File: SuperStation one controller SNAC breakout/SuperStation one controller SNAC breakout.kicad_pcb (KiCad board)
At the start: 2 copper layers, 50 x 100 mm, 28 parts, among them J1 Conn_01x09_Socket, J2 Conn_01x09_Socket, J3 USB3_A, Q1 BSS138, Q2 BSS138, Q3 BSS138, Q4 BSS138, Q5 BSS138, Q6 BSS138, Q7 BSS138, U1 NCP1117-5.0_SOT223

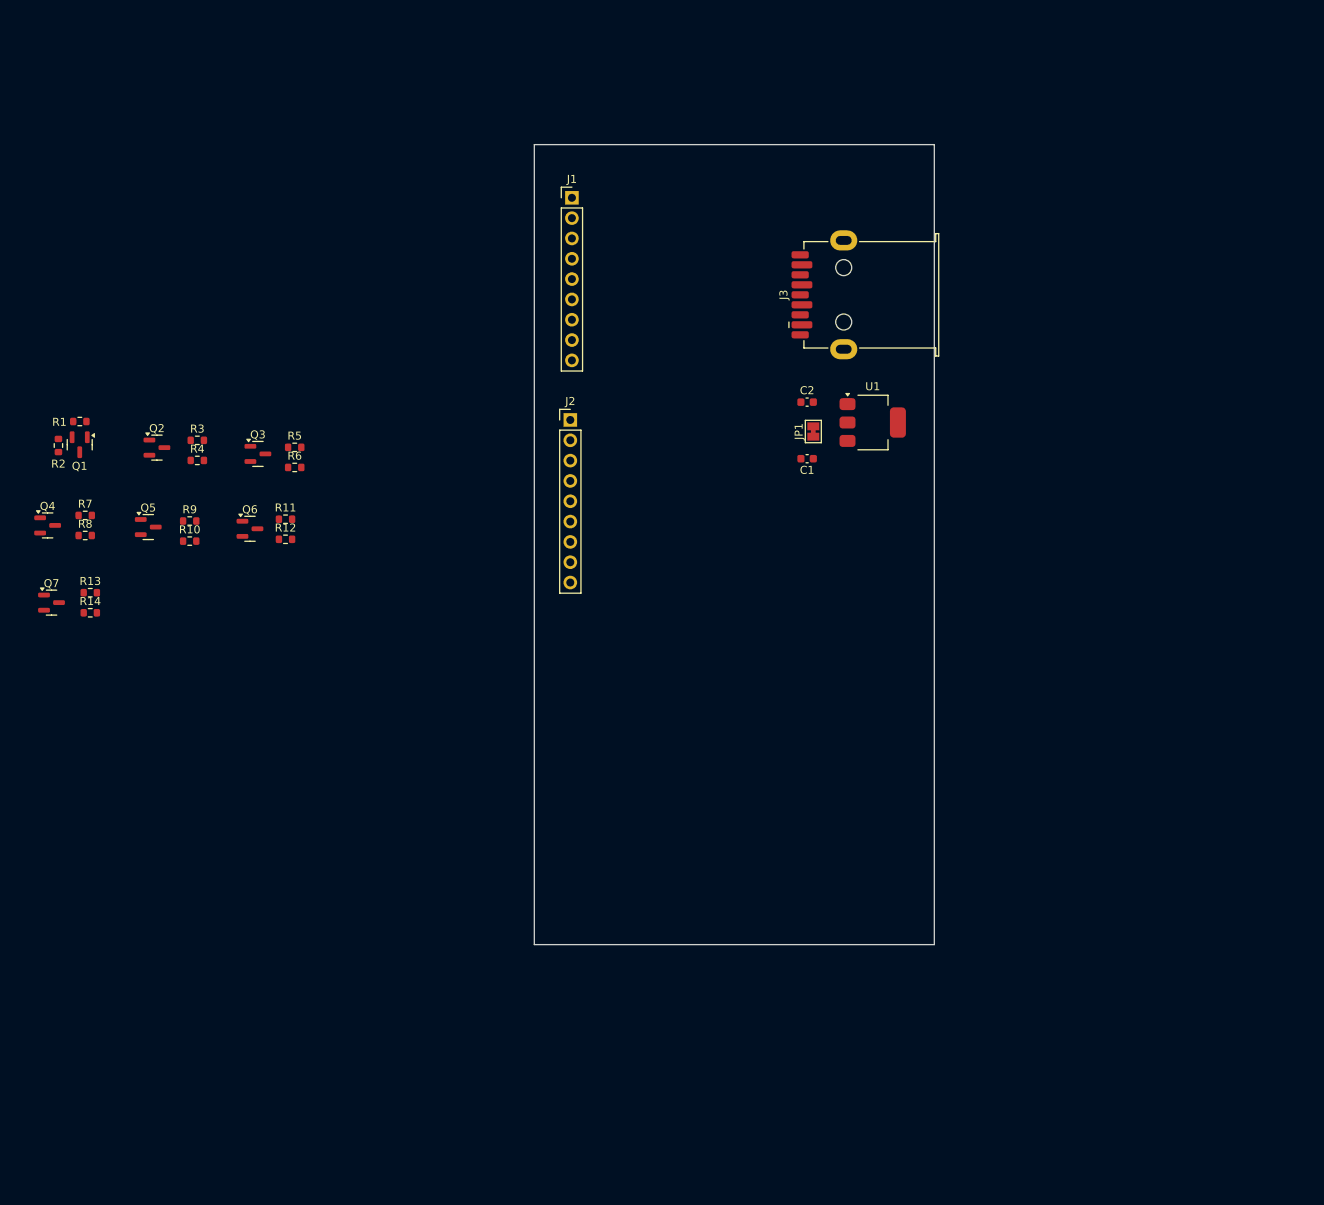
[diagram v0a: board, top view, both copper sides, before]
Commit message: added power sheet to schematic and started rough pcb placement
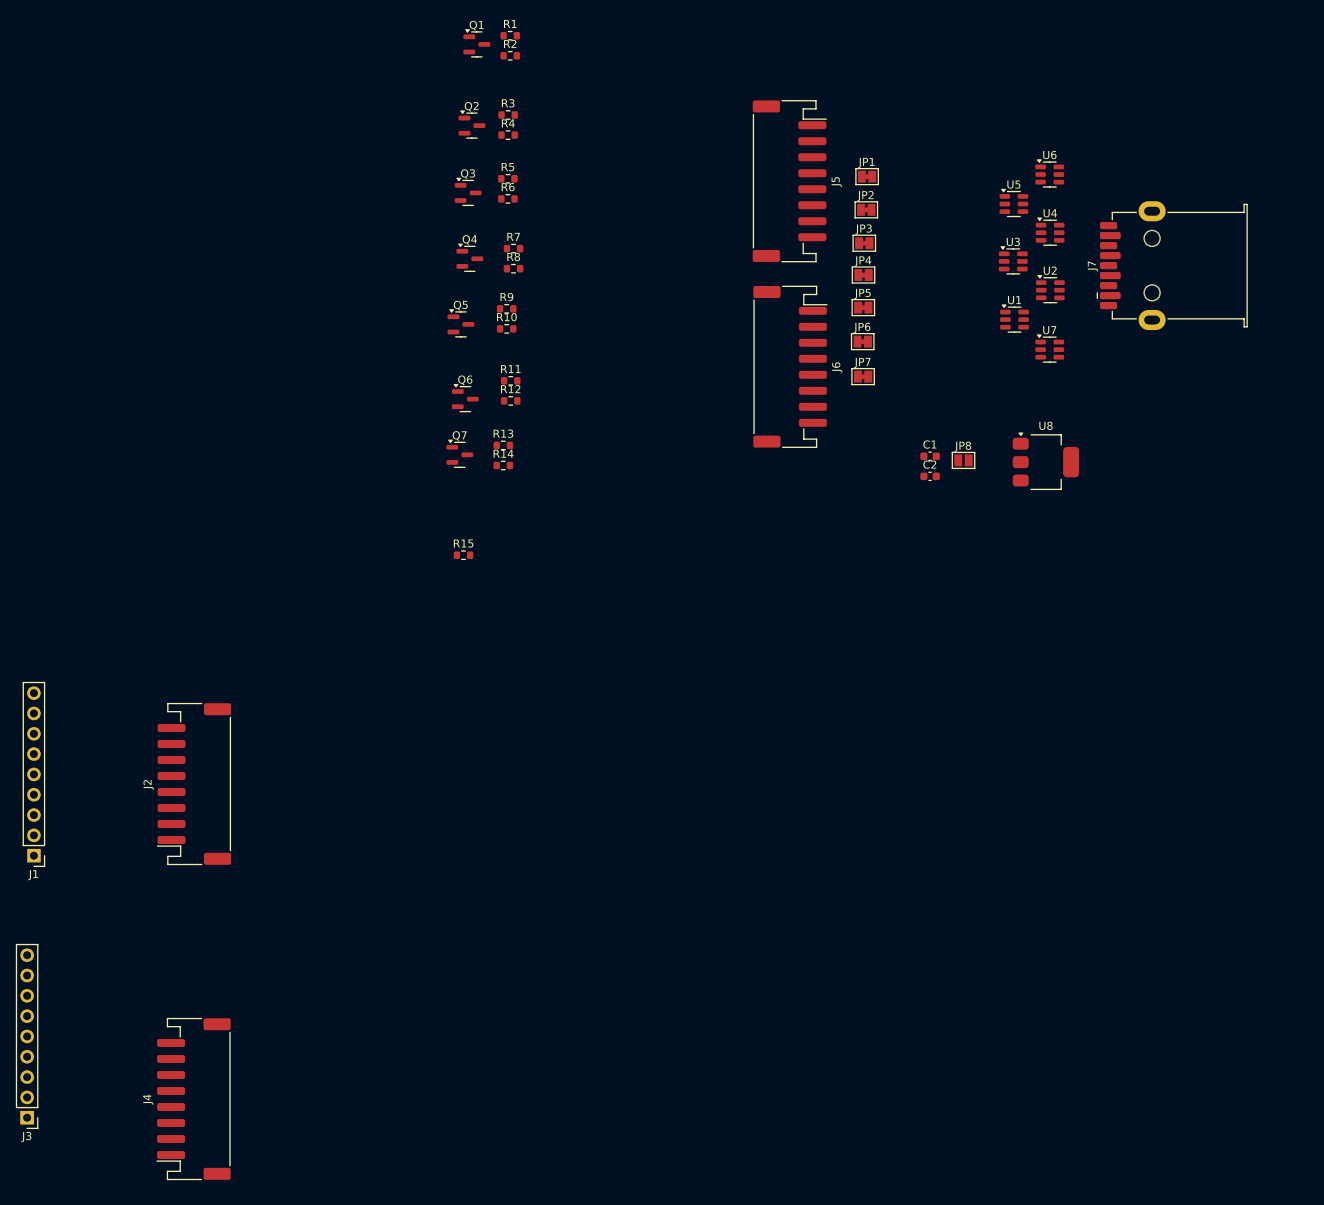
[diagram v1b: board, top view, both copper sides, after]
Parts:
- added J4: Conn_01x09_Pin, Connector_JST:JST_PH_S8B-PH-SM4-TB_1x08-1MP_P2.00mm_Horizontal, F.Cu at (57.3, 169.1)
- added J5: Conn_01x09_Pin, Connector_JST:JST_PH_S8B-PH-SM4-TB_1x08-1MP_P2.00mm_Horizontal, F.Cu at (131.7, 54.4)
- added J6: Conn_01x09_Pin, Connector_JST:JST_PH_S8B-PH-SM4-TB_1x08-1MP_P2.00mm_Horizontal, F.Cu at (131.8, 77.6)
- added J7: USB3_A, Connector_USB:USB3_A_Receptacle_Wuerth_692122030100, F.Cu at (180.5, 65.0)
- added JP2: Jumper_2_Bridged, Jumper:SolderJumper-2_P1.3mm_Bridged_Pad1.0x1.5mm, F.Cu at (141.3, 58.0)
- added JP3: Jumper_2_Bridged, Jumper:SolderJumper-2_P1.3mm_Bridged_Pad1.0x1.5mm, F.Cu at (141.1, 62.1)
- added JP4: Jumper_2_Bridged, Jumper:SolderJumper-2_P1.3mm_Bridged_Pad1.0x1.5mm, F.Cu at (141.0, 66.1)
- added JP5: Jumper_2_Bridged, Jumper:SolderJumper-2_P1.3mm_Bridged_Pad1.0x1.5mm, F.Cu at (140.9, 70.2)
- added JP6: Jumper_2_Bridged, Jumper:SolderJumper-2_P1.3mm_Bridged_Pad1.0x1.5mm, F.Cu at (140.9, 74.5)
- added JP7: Jumper_2_Bridged, Jumper:SolderJumper-2_P1.3mm_Bridged_Pad1.0x1.5mm, F.Cu at (140.9, 78.8)
- added JP8: Jumper_2_Open, Jumper:SolderJumper-2_P1.3mm_Open_Pad1.0x1.5mm, F.Cu at (153.5, 89.3)
- added R15: 10k, Resistor_SMD:R_0603_1608Metric, F.Cu at (91.0, 101.2)
- added U2: SN74LVC1G3157, Package_TO_SOT_SMD:TSOT-23-6, F.Cu at (164.3, 68.0)
- added U3: SN74LVC1G3157, Package_TO_SOT_SMD:TSOT-23-6, F.Cu at (159.7, 64.4)
- added U4: SN74LVC1G3157, Package_TO_SOT_SMD:TSOT-23-6, F.Cu at (164.3, 60.8)
- added U5: SN74LVC1G3157, Package_TO_SOT_SMD:TSOT-23-6, F.Cu at (159.8, 57.2)
- added U6: SN74LVC1G3157, Package_TO_SOT_SMD:TSOT-23-6, F.Cu at (164.2, 53.6)
- added U7: SN74LVC1G3157, Package_TO_SOT_SMD:TSOT-23-6, F.Cu at (164.2, 75.5)
- added U8: NCP1117-5.0_SOT223, Package_TO_SOT_SMD:SOT-223-3_TabPin2, F.Cu at (163.8, 89.5)
- J1: value Conn_01x09_Socket -> ~
- J2: value Conn_01x09_Socket -> Conn_01x09_Pin; footprint Connector_PinHeader_2.54mm:PinHeader_1x09_P2.54mm_Vertical -> Connector_JST:JST_PH_S8B-PH-SM4-TB_1x08-1MP_P2.00mm_Horizontal
- J3: value USB3_A -> ~; footprint Connector_USB:USB3_A_Receptacle_Wuerth_692122030100 -> Connector_PinHeader_2.54mm:PinHeader_1x09_P2.54mm_Vertical
- U1: value NCP1117-5.0_SOT223 -> SN74LVC1G3157; footprint Package_TO_SOT_SMD:SOT-223-3_TabPin2 -> Package_TO_SOT_SMD:TSOT-23-6
- moved J3 147.4 mm to (36.4, 171.5), turned to 180 degrees
- moved J1 106.2 mm to (37.3, 138.7), turned to 180 degrees
- moved R2 74.6 mm to (96.8, 38.7), turned to 0 degrees
- moved R1 72.3 mm to (96.8, 36.2), turned to 0 degrees
- moved Q1 70.5 mm to (92.6, 37.3), turned to 0 degrees
- moved J2 65.4 mm to (57.3, 129.8), turned to 90 degrees
- moved R7 63.1 mm to (97.2, 62.8)
- moved R8 63.1 mm to (97.2, 65.3)
- moved Q4 62.4 mm to (91.8, 64.1)
- moved Q2 56.3 mm to (92.0, 47.5)
- moved R3 56.2 mm to (96.5, 46.1)
- moved R4 56.2 mm to (96.5, 48.6)
- moved R13 54.8 mm to (96.0, 87.4)
- moved R14 54.8 mm to (96.0, 89.9)
- moved Q7 54.3 mm to (90.5, 88.6)
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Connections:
- C1 pad 1: V_RUMBLE -> +7.5V
- J1 pad 1: LV3 -> /PS Input Breakout/ACK_P1
- J1 pad 2: LV7 -> /PS Input Breakout/IRQ10_P1
- J1 pad 3: LV6 -> /PS Input Breakout/CLK_P1
- J1 pad 4: LV2 -> /PS Input Breakout/ATT_P1
- J1 pad 5: +3.3V -> +3.3V_P1
- J1 pad 6: GND -> GND_P1
- J1 pad 7: V_RUMBLE -> +7.5V_P1
- J1 pad 8: LV1 -> /PS Input Breakout/CMD_P1
- J1 pad 9: LV5 -> /PS Input Breakout/DAT_P1
- J2 pad 1: LV3 -> +3.3V_P1
- J2 pad 2: LV7 -> +7.5V_P1
- J2 pad 3: LV6 -> /PS Input Breakout/ACK_P1
- J2 pad 4: LV4 -> /PS Input Breakout/IRQ10_P1
- J2 pad 5: +3.3V -> /PS Input Breakout/CLK_P1
- J2 pad 6: GND -> /PS Input Breakout/ATT_P1
- J2 pad 7: V_RUMBLE -> /PS Input Breakout/CMD_P1
- J2 pad 8: LV1 -> /PS Input Breakout/DAT_P1
- J3 pad 1: +5V -> /PS Input Breakout/ACK_P2
- J3 pad 2: HV2 -> /PS Input Breakout/IRQ10_P2
- J3 pad 3: HV4 -> /PS Input Breakout/CLK_P2
- J3 pad 4: GND -> /PS Input Breakout/ATT_P2
- J3 pad 5: HV6 -> +3.3V_P2
- J3 pad 6: HV5 -> GND_P2
- J3 pad 7: HV3 -> +7.5V_P2
- J3 pad 8: HV1 -> /PS Input Breakout/CMD_P2
- J3 pad 9: HV7 -> /PS Input Breakout/DAT_P2
- JP1 pad 1: V_RUMBLE -> /SNAC/ACK
- JP1 pad 2: +5V -> /SNAC/LV3
- Q1 pad 2: LV1 -> /SNAC/LV1
- Q1 pad 3: HV1 -> /SNAC/HV1
- Q2 pad 2: LV2 -> /SNAC/LV2
- Q2 pad 3: HV2 -> /SNAC/HV2
- Q3 pad 2: LV3 -> /SNAC/LV3
- Q3 pad 3: HV3 -> /SNAC/HV3
- Q4 pad 2: LV4 -> /SNAC/LV4
- Q4 pad 3: HV4 -> /SNAC/HV4
- Q5 pad 2: LV5 -> /SNAC/LV5
- Q5 pad 3: HV5 -> /SNAC/HV5
- Q6 pad 2: LV6 -> /SNAC/LV6
- Q6 pad 3: HV6 -> /SNAC/HV6
- Q7 pad 2: LV7 -> /SNAC/LV7
- Q7 pad 3: HV7 -> /SNAC/HV7
- R1 pad 2: LV1 -> /SNAC/LV1
- R10 pad 2: HV5 -> /SNAC/HV5
- R11 pad 2: LV6 -> /SNAC/LV6
- R12 pad 2: HV6 -> /SNAC/HV6
- R13 pad 2: LV7 -> /SNAC/LV7
- R14 pad 2: HV7 -> /SNAC/HV7
- R2 pad 2: HV1 -> /SNAC/HV1
- R3 pad 2: LV2 -> /SNAC/LV2
- R4 pad 2: HV2 -> /SNAC/HV2
- R5 pad 2: LV3 -> /SNAC/LV3
- R6 pad 2: HV3 -> /SNAC/HV3
- R7 pad 2: LV4 -> /SNAC/LV4
- R8 pad 2: HV4 -> /SNAC/HV4
- R9 pad 2: LV5 -> /SNAC/LV5
- U1 pad 1: GND -> /SNAC/HV1
- U1 pad 2: +5V -> GND
- U1 pad 3: V_RUMBLE -> /SNAC/LV1
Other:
- board outline removed

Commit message: board layout and added debug breakouts for all signals
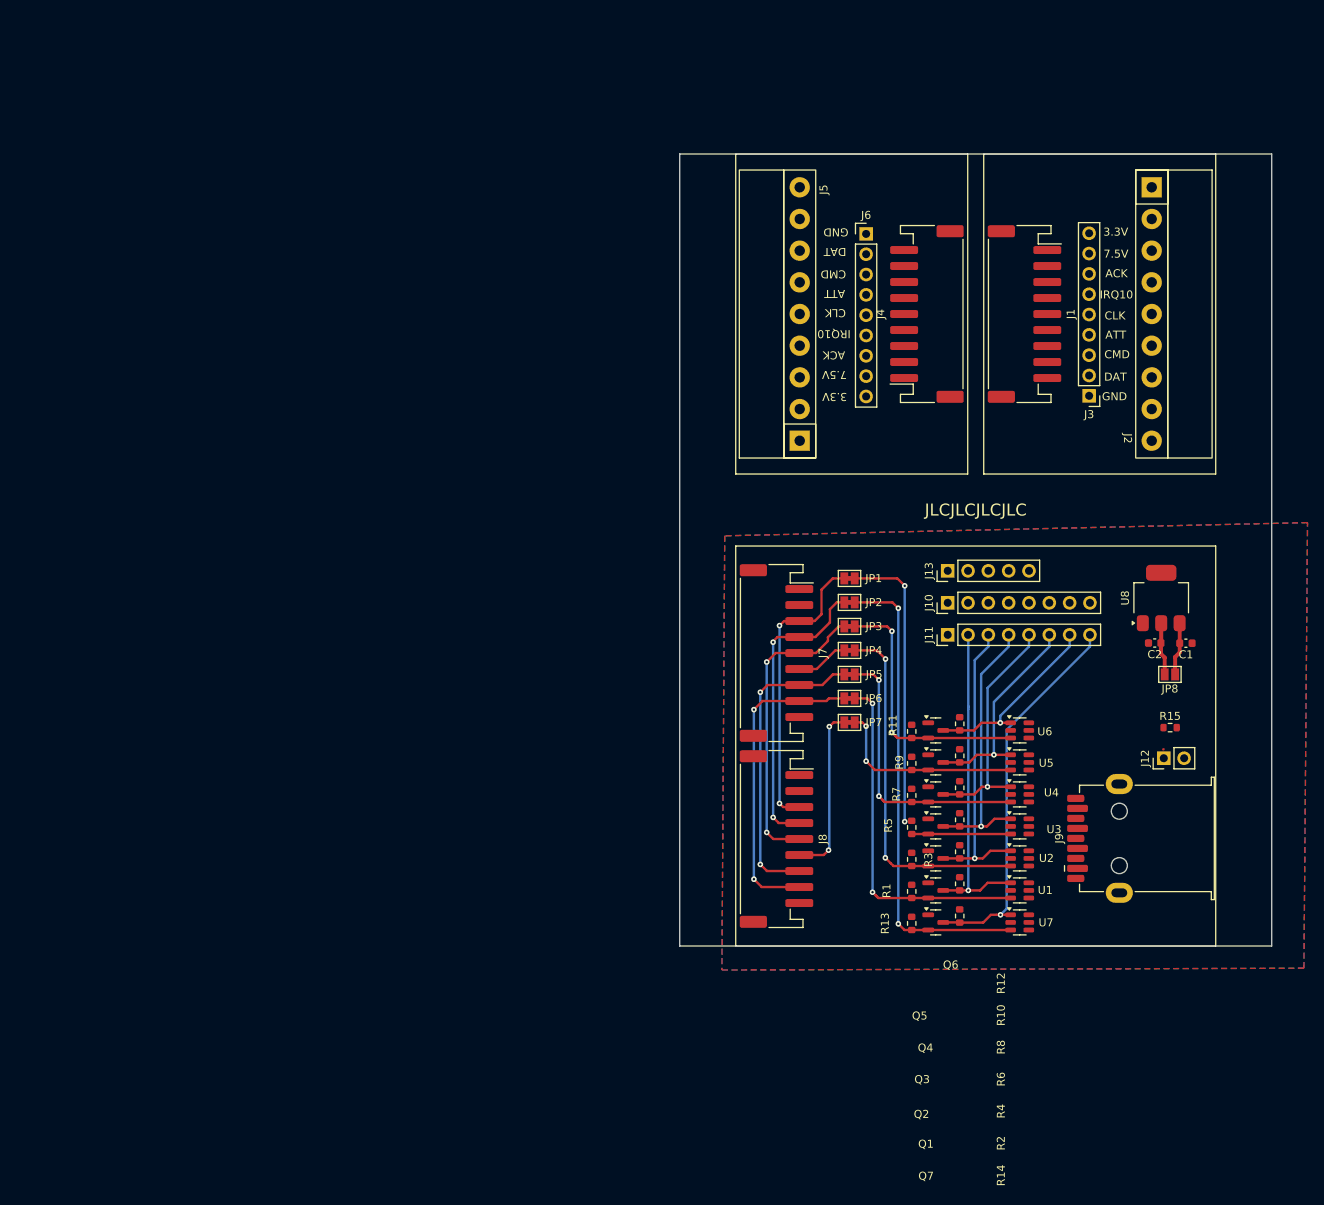
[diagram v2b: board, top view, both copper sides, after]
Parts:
- removed the J1 at (37.3, 138.7)
- added J10: Conn_01x08_Pin, Connector_PinHeader_2.54mm:PinHeader_1x08_P2.54mm_Vertical, F.Cu at (151.5, 107.1)
- added J11: Conn_01x08_Pin, Connector_PinHeader_2.54mm:PinHeader_1x08_P2.54mm_Vertical, F.Cu at (151.5, 111.1)
- added J12: Conn_01x02_Pin, Connector_PinHeader_2.54mm:PinHeader_1x02_P2.54mm_Vertical, F.Cu at (178.5, 126.5)
- added J13: Conn_01x05_Pin, Connector_PinHeader_2.54mm:PinHeader_1x05_P2.54mm_Vertical, F.Cu at (151.5, 103.1)
- added J2: PlayStation Con 1P, Nick_Connectors:PlayStation 1P, F.Cu at (177.0, 71.0)
- added J5: PlayStation Con 1P, Nick_Connectors:PlayStation 1P, F.Cu at (133.0, 71.0)
- added J6: Conn_01x09_Pin, Connector_PinHeader_2.54mm:PinHeader_1x09_P2.54mm_Vertical, F.Cu at (141.3, 61.0)
- J1: renamed from J2; value Conn_01x09_Pin -> JST-PH; footprint Connector_JST:JST_PH_S8B-PH-SM4-TB_1x08-1MP_P2.00mm_Horizontal -> Connector_JST:JST_PH_S9B-PH-SM4-TB_1x09-1MP_P2.00mm_Horizontal
- J3: value ~ -> Conn_01x09_Pin
- J4: value Conn_01x09_Pin -> JST-PH; footprint Connector_JST:JST_PH_S8B-PH-SM4-TB_1x08-1MP_P2.00mm_Horizontal -> Connector_JST:JST_PH_S9B-PH-SM4-TB_1x09-1MP_P2.00mm_Horizontal
- J7: renamed from J5; value Conn_01x09_Pin -> JST-PH; footprint Connector_JST:JST_PH_S8B-PH-SM4-TB_1x08-1MP_P2.00mm_Horizontal -> Connector_JST:JST_PH_S9B-PH-SM4-TB_1x09-1MP_P2.00mm_Horizontal
- J8: renamed from J6; value Conn_01x09_Pin -> JST-PH; footprint Connector_JST:JST_PH_S8B-PH-SM4-TB_1x08-1MP_P2.00mm_Horizontal -> Connector_JST:JST_PH_S9B-PH-SM4-TB_1x09-1MP_P2.00mm_Horizontal
- moved J3 160.5 mm to (169.2, 81.2)
- moved J4 134.3 mm to (148.9, 71.0)
- moved Q1 120.3 mm to (150.0, 143.1)
- moved J1 119.3 mm to (161.1, 71.0), turned to -90 degrees
- moved R1 118.2 mm to (147.0, 143.2), turned to -90 degrees
- moved R2 117.8 mm to (153.0, 142.2), turned to -90 degrees
- moved Q2 108.4 mm to (150.0, 139.1)
- moved R4 105.9 mm to (153.0, 138.2), turned to -90 degrees
- moved R3 105.8 mm to (147.0, 139.2), turned to -90 degrees
- moved Q3 98.4 mm to (150.0, 135.1)
- moved R6 96.0 mm to (153.0, 134.2), turned to -90 degrees
- moved R5 95.5 mm to (147.0, 135.2), turned to -90 degrees
- moved R15 90.9 mm to (179.3, 122.7)
- moved Q4 88.7 mm to (150.0, 131.1)
- moved R8 85.6 mm to (153.0, 130.2), turned to -90 degrees
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- renumbered J7 to J9
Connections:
- J1 pad MP: (no net) -> GND_P1
- J3 pad 1: /PS Input Breakout/ACK_P2 -> GND_P1
- J3 pad 2: /PS Input Breakout/IRQ10_P2 -> /PS Input Breakout/DAT_P1
- J3 pad 3: /PS Input Breakout/CLK_P2 -> /PS Input Breakout/CMD_P1
- J3 pad 4: /PS Input Breakout/ATT_P2 -> /PS Input Breakout/ATT_P1
- J3 pad 5: +3.3V_P2 -> /PS Input Breakout/CLK_P1
- J3 pad 6: GND_P2 -> /PS Input Breakout/IRQ10_P1
- J3 pad 7: +7.5V_P2 -> /PS Input Breakout/ACK_P1
- J3 pad 8: /PS Input Breakout/CMD_P2 -> +7.5V_P1
- J3 pad 9: /PS Input Breakout/DAT_P2 -> +3.3V_P1
- J4 pad MP: (no net) -> GND_P2
- J7 pad MP: (no net) -> GND
- J8 pad MP: (no net) -> GND
- R15 pad 2: GND -> +5V
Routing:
- net /SNAC/LV7: track 0.00 -> 59.6 mm, vias 0 -> 2
- net /SNAC/LV3: track 0.00 -> 48.5 mm, vias 0 -> 2
- net /SNAC/HV7: track 0.00 -> 48.5 mm, vias 0 -> 1
- net /SNAC/LV2: track 0.00 -> 45.2 mm, vias 0 -> 2
- net /SNAC/LV1: track 0.00 -> 43.9 mm, vias 0 -> 2
- net /SNAC/HV1: track 0.00 -> 40.9 mm, vias 0 -> 1
- net /SNAC/DAT: track 0.00 -> 39.2 mm, vias 0 -> 2
- net /SNAC/CMD: track 0.00 -> 38.2 mm, vias 0 -> 2
- net /SNAC/HV2: track 0.00 -> 37.6 mm, vias 0 -> 1
- net /SNAC/CLK: track 0.00 -> 37.5 mm, vias 0 -> 2
- net /SNAC/IRQ10: track 0.00 -> 37.5 mm, vias 0 -> 2
- net /SNAC/ACK: track 0.00 -> 37.2 mm, vias 0 -> 2
- net /SNAC/LV4: track 0.00 -> 34.8 mm, vias 0 -> 2
- net /SNAC/HV3: track 0.00 -> 34.2 mm, vias 0 -> 1
- net /SNAC/LV6: track 0.00 -> 32.9 mm, vias 0 -> 2
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- added copper zone on B.Cu, net GND
- added copper zone on F.Cu, net GND
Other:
- board outline added: 74 x 99 mm
- board text added: "3.3V"
- board text added: "7.5V"
- board text added: "ACK"
- board text added: "ATT"
- board text added: "CLK"
- board text added: "CMD"
- board text added: "DAT"
- board text added: "GND"
- board text added: "IRQ10"
- board text added: "JLCJLCJLCJLC"
- board text added: "V-CUT"

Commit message: completed board layout
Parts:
- moved J13 30.4 mm to (181.8, 103.8), turned to 0 degrees
- moved R15 17.0 mm to (162.5, 120.2)
- moved J12 16.9 mm to (164.2, 117.5), turned to -90 degrees
- moved U8 16.7 mm to (172.8, 122.3), turned to 180 degrees
- moved C2 11.1 mm to (178.4, 123.2), turned to -90 degrees
- moved C1 7.66 mm to (178.4, 119.2), turned to 90 degrees
- moved JP8 5.31 mm to (180.5, 121.2), turned to -90 degrees
- moved J10 4.10 mm to (151.6, 103.0)
- moved J3 0.68 mm to (168.5, 81.2)
- moved J6 0.25 mm to (141.5, 60.8)
- moved J11 0.11 mm to (151.6, 111.0)
- renumbered JP6 to JP1, JP4 to JP2, JP1 to JP3, JP5 to JP4, JP7 to JP5, JP3 to JP6, JP2 to JP7
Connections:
- J12 pad 1: /SNAC/MUX_SWITCH -> GND
- J12 pad 2: GND -> /SNAC/MUX_SWITCH
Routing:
- net +3.3V: track 0.00 -> 163.4 mm, vias 0 -> 9
- net +5V: track 6.61 -> 141.9 mm, vias 0 -> 15
- net +7.5V: track 6.64 -> 99.2 mm, vias 0 -> 2
- net /SNAC/MUX_SWITCH: track 0.04 -> 62.3 mm, vias 0 -> 7
- net /SNAC/LV5: track 24.5 -> 61.9 mm, vias 2 -> 4
- net /SNAC/LV4: track 34.8 -> 65.3 mm, vias 2 -> 4
- net /SNAC/LV7: track 59.6 -> 88.7 mm, vias 2 -> 3
- net /SNAC/LV1: track 43.9 -> 71.1 mm, vias 2 -> 4
- net /SNAC/LV6: track 32.9 -> 59.2 mm
- net +7.5V_P2: track 0.00 -> 24.3 mm
- net +7.5V_P1: track 0.00 -> 24.3 mm
- net /SNAC/LV2: track 45.2 -> 68.1 mm, vias 2 -> 4
- net /PS Input Breakout/ACK_P2: track 0.00 -> 20.5 mm
- net /PS Input Breakout/ACK_P1: track 0.00 -> 20.3 mm
- net +3.3V_P1: track 0.00 -> 19.1 mm
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- added copper zone on B.Cu, net GND_P1
- added copper zone on F.Cu, net GND_P1
- added copper zone on B.Cu, net GND_P2
- added copper zone on F.Cu, net GND_P2
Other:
- board text added: "HV"
- board text added: "LV"

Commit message: replaced voltage regulator with a cheaper and smaller alternative. The same that is on all opensource SNAC adapters.
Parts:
- removed U8: NCP1117-5.0_SOT223, Package_TO_SOT_SMD:SOT-223-3_TabPin2
- added U9: XC6206P332MR, Package_TO_SOT_SMD:SOT-23-3, F.Cu at (177.4, 120.5)
- moved JP8 5.09 mm to (177.4, 125.3), turned to 180 degrees
- moved C1 3.92 mm to (179.3, 123.0), turned to 0 degrees
- moved C2 2.85 mm to (175.5, 123.1), turned to 180 degrees
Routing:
- net +5V: track 141.9 -> 147.7 mm
- net GND: vias 221 -> 186
